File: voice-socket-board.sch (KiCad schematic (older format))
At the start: 296 parts, among them J1 JACK_MONO_SW, J2 JACK_MONO_SW, J3 JACK_MONO_SW, P1 CONN_01X03, P2 CONN_01X03, P3 CONN_02X05, P4 DDR3-DIMM, Q1 MMBT3904, Q10 MMBT3906, Q2 DMMT3904W, Q3 2N7002, Q4 2N7002, Q5 MMBT3904, Q6 MMBT3906, Q7 MMBT3904, Q8 MMBT3904, Q9 MMBT3904, SW1 SPST, SW10 SP3T, SW11 SP3T, SW12 SP3T, SW13 SP3T, SW14 SPST, SW15 TACT_SWITCH, SW16 SP3T, SW2 SPST, SW3 SP3T, SW4 SP3T, SW5 SPST, SW6 SPST, SW7 Switch_SPDT_x2, SW8 2P3T, SW9 SP3T, U1 LM833, U10 TL072-, U11 NE5534, U2 TL072-, U3 TL072-, U4 TL072-, U5 TL072-, U6 TL072-, U7 MAX9945, U8 CD4013, U9 TL072-

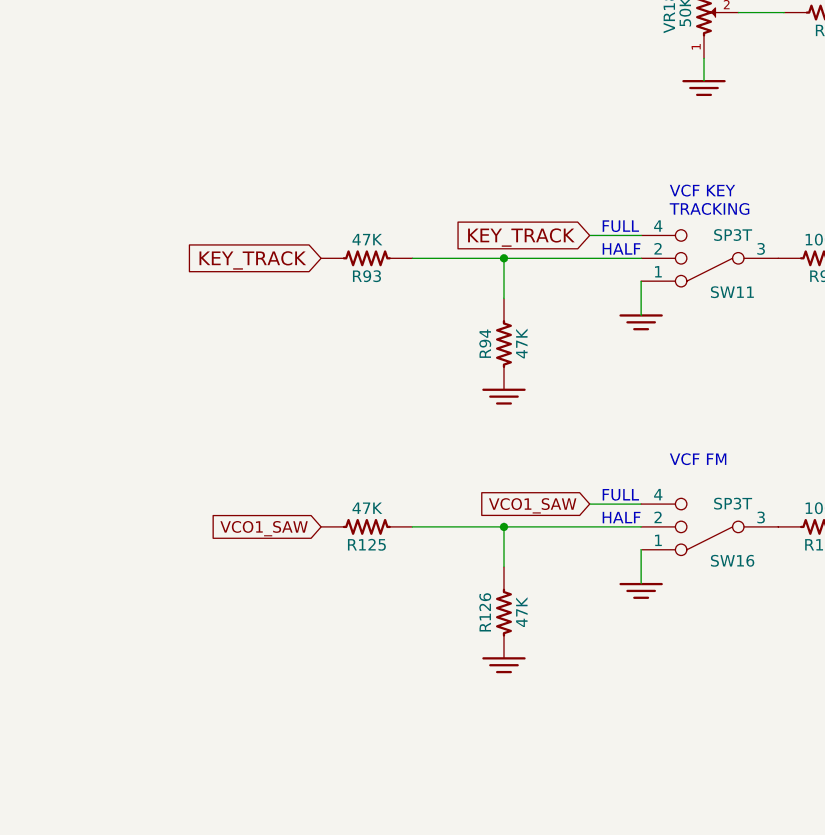
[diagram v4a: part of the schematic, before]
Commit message: changed FM and key tracking inputs into filter cutoff summer
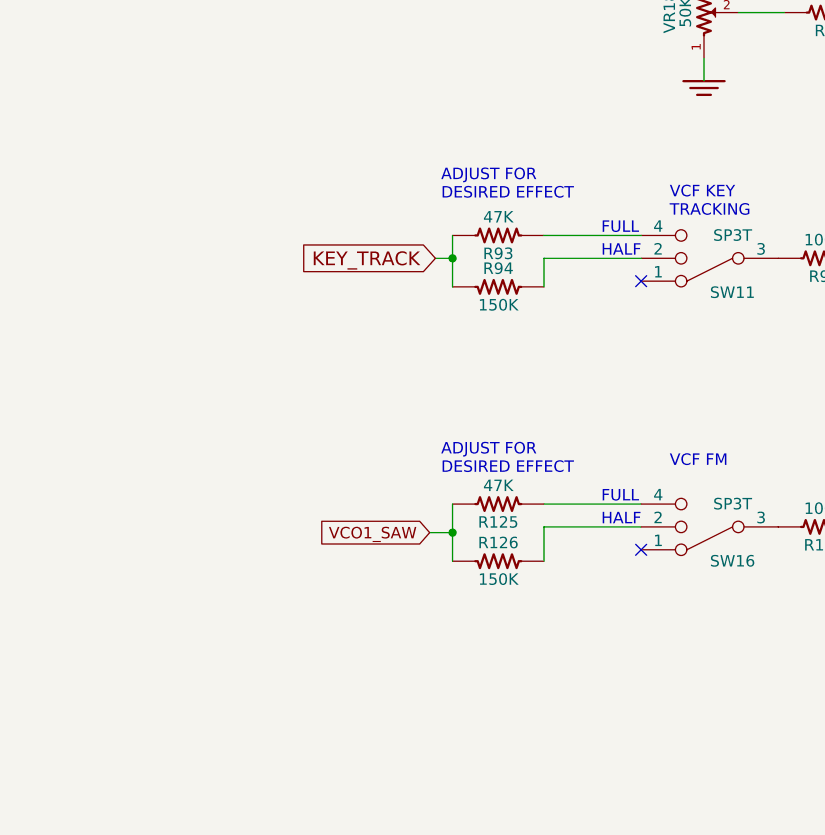
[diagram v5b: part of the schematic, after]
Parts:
- R126, R94: value 47K -> 150K
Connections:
- net GND: no longer R126.1, R94.1, SW11.1, SW16.1
- net KEY_TRACK: now also R94.1; no longer SW11.4
- net VCO1_SAW: now also R126.1; no longer SW16.4
- net at R94.2, SW11.2: no longer R93.1
- net at R126.2, SW16.2: no longer R125.1
- new net: R93.1, SW11.4
- new net: R125.1, SW16.4
- no-connect marks 11 -> 13
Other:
- note added: "ADJUST FOR \nDESIRED EFFECT\n"
- moved on the sheet: R125, R126, R93, R94
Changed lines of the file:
@@
 Text Notes 33525 16700 0    50   ~ 0
 OR SOME OTHER LOW OFFSET PRECISION OP AMP
-Text GLabel 18075 23925 0    60   Input ~ 0
-KEY_TRACK
 $Comp
 L SP3T SW11
@@
 $EndComp
 $Comp
-L GND_E #PWR0222
-U 1 1 566E42FA
-P 18300 24275
-F 0 "#PWR0222" V 18300 24275 30  0001 C CNN
-F 1 "GND_E" H 18300 24205 30  0001 C CNN
-F 2 "" H 18300 24275 60  0000 C CNN
-F 3 "" H 18300 24275 60  0000 C CNN
-	1    18300 24275
-	1    0    0    -1
-$EndComp
-$Comp
 L R_US R98
 U 1 1 566E8731
@@
 	0    1    1    0
 $EndComp
-Text GLabel 16900 24025 0    60   Input ~ 0
+Text GLabel 17400 24025 0    60   Input ~ 0
 KEY_TRACK
 $Comp
 L R_US R93
 U 1 1 566EB837
-P 17100 24025
-F 0 "R93" V 17180 24025 50  0000 C CNN
-F 1 "47K" V 17020 24025 50  0000 C CNN
-F 2 "MyModules:SM0603-R-JRL" H 17100 24025 60  0001 C CNN
-F 3 "" H 17100 24025 60  0000 C CNN
-	1    17100 24025
+P 17675 23925
+F 0 "R93" V 17755 23925 50  0000 C CNN
+F 1 "47K" V 17595 23925 50  0000 C CNN
+F 2 "MyModules:SM0603-R-JRL" H 17675 23925 60  0001 C CNN
+F 3 "" H 17675 23925 60  0000 C CNN
+	1    17675 23925
 	0    1    1    0
 $EndComp
@@
 L R_US R94
 U 1 1 566EBBBE
-P 17700 24400
-F 0 "R94" V 17780 24400 50  0000 C CNN
-F 1 "47K" V 17620 24400 50  0000 C CNN
-F 2 "MyModules:SM0603-R-JRL" H 17700 24400 60  0001 C CNN
-F 3 "" H 17700 24400 60  0000 C CNN
-	1    17700 24400
-	-1   0    0    1
-$EndComp
-$Comp
-L GND_E #PWR0223
-U 1 1 566ED5F9
-P 17700 24600
-F 0 "#PWR0223" V 17700 24600 30  0001 C CNN
-F 1 "GND_E" H 17700 24530 30  0001 C CNN
-F 2 "" H 17700 24600 60  0000 C CNN
-F 3 "" H 17700 24600 60  0000 C CNN
-	1    17700 24600
-	1    0    0    -1
+P 17675 24150
+F 0 "R94" V 17755 24150 50  0000 C CNN
+F 1 "150K" V 17595 24150 50  0000 C CNN
+F 2 "MyModules:SM0603-R-JRL" H 17675 24150 60  0001 C CNN
+F 3 "" H 17675 24150 60  0000 C CNN
+	1    17675 24150
+	0    -1   -1   0
 $EndComp
 Text Notes 18425 23850 0    50   ~ 0
@@
 Connection ~ 29875 16750
 Wire Wire Line
-	18300 24125 18300 24275
-Wire Wire Line
-	18300 23925 18075 23925
+	17875 23925 18300 23925
 Wire Wire Line
 	19300 24025 19575 24025
 Connection ~ 19575 24025
-Wire Wire Line
-	17300 24025 18300 24025
-Wire Wire Line
-	17700 24200 17700 24025
-Connection ~ 17700 24025
 Wire Wire Line
 	28125 10325 29025 10325
@@
 $EndComp
 $Comp
-L GND_E #PWR0242
-U 1 1 567C7030
-P 18300 25450
-F 0 "#PWR0242" V 18300 25450 30  0001 C CNN
-F 1 "GND_E" H 18300 25380 30  0001 C CNN
-F 2 "" H 18300 25450 60  0000 C CNN
-F 3 "" H 18300 25450 60  0000 C CNN
-	1    18300 25450
-	1    0    0    -1
-$EndComp
-$Comp
 L R_US R127
 U 1 1 567C7036
@@
 L R_US R125
 U 1 1 567C703D
-P 17100 25200
-F 0 "R125" V 17180 25200 50  0000 C CNN
-F 1 "47K" V 17020 25200 50  0000 C CNN
-F 2 "MyModules:SM0603-R-JRL" H 17100 25200 60  0001 C CNN
-F 3 "" H 17100 25200 60  0000 C CNN
-	1    17100 25200
+P 17675 25100
+F 0 "R125" V 17755 25100 50  0000 C CNN
+F 1 "47K" V 17595 25100 50  0000 C CNN
+F 2 "MyModules:SM0603-R-JRL" H 17675 25100 60  0001 C CNN
+F 3 "" H 17675 25100 60  0000 C CNN
+	1    17675 25100
 	0    1    1    0
 $EndComp
@@
 L R_US R126
 U 1 1 567C7043
-P 17700 25575
-F 0 "R126" V 17780 25575 50  0000 C CNN
-F 1 "47K" V 17620 25575 50  0000 C CNN
-F 2 "MyModules:SM0603-R-JRL" H 17700 25575 60  0001 C CNN
-F 3 "" H 17700 25575 60  0000 C CNN
-	1    17700 25575
-	-1   0    0    1
-$EndComp
-$Comp
-L GND_E #PWR0243
-U 1 1 567C7049
-P 17700 25775
-F 0 "#PWR0243" V 17700 25775 30  0001 C CNN
-F 1 "GND_E" H 17700 25705 30  0001 C CNN
-F 2 "" H 17700 25775 60  0000 C CNN
-F 3 "" H 17700 25775 60  0000 C CNN
-	1    17700 25775
-	1    0    0    -1
+P 17675 25350
+F 0 "R126" V 17755 25350 50  0000 C CNN
+F 1 "150K" V 17595 25350 50  0000 C CNN
+F 2 "MyModules:SM0603-R-JRL" H 17675 25350 60  0001 C CNN
+F 3 "" H 17675 25350 60  0000 C CNN
+	1    17675 25350
+	0    -1   -1   0
 $EndComp
 Text Notes 18425 25025 0    50   ~ 0
 VCF FM\n\n
 Wire Wire Line
-	18300 25300 18300 25450
-Wire Wire Line
-	18300 25100 18075 25100
-Wire Wire Line
-	17300 25200 18300 25200
-Wire Wire Line
-	17700 25375 17700 25200
-Connection ~ 17700 25200
+	17875 25100 18300 25100
 Text Notes 18125 25100 0    50   ~ 0
 FULL\n
 Text Notes 18125 25200 0    50   ~ 0
 HALF
-Text GLabel 16900 25200 0    50   Input ~ 0
-VCO1_SAW
-Text GLabel 18075 25100 0    50   Input ~ 0
+Text GLabel 17375 25225 0    50   Input ~ 0
 VCO1_SAW
 Wire Wire Line
@@
 $EndComp
 $Comp
-L GND_E #PWR0246
+L GND_E #PWR0244
 U 1 1 567F81C4
 P 26575 23750
-F 0 "#PWR0246" V 26575 23750 30  0001 C CNN
+F 0 "#PWR0244" V 26575 23750 30  0001 C CNN
 F 1 "GND_E" H 26575 23680 30  0001 C CNN
 F 2 "" H 26575 23750 60  0000 C CNN
@@
 Wire Wire Line
 	27325 25300 27325 25575
+Wire Wire Line
+	18300 24025 17875 24025
+Wire Wire Line
+	17875 24025 17875 24150
+Wire Wire Line
+	17475 23925 17475 24150
+Wire Wire Line
+	17400 24025 17475 24025
+Connection ~ 17475 24025
+NoConn ~ 18300 24125
+Text Notes 17425 23775 0    50   ~ 0
+ADJUST FOR \nDESIRED EFFECT\n
+NoConn ~ 18300 25300
+Wire Wire Line
+	18300 25200 17875 25200
+Wire Wire Line
+	17875 25200 17875 25350
+Wire Wire Line
+	17475 25100 17475 25350
+Wire Wire Line
+	17375 25225 17475 25225
+Connection ~ 17475 25225
+Text Notes 17425 24975 0    50   ~ 0
+ADJUST FOR \nDESIRED EFFECT\n
 $EndSCHEMATC

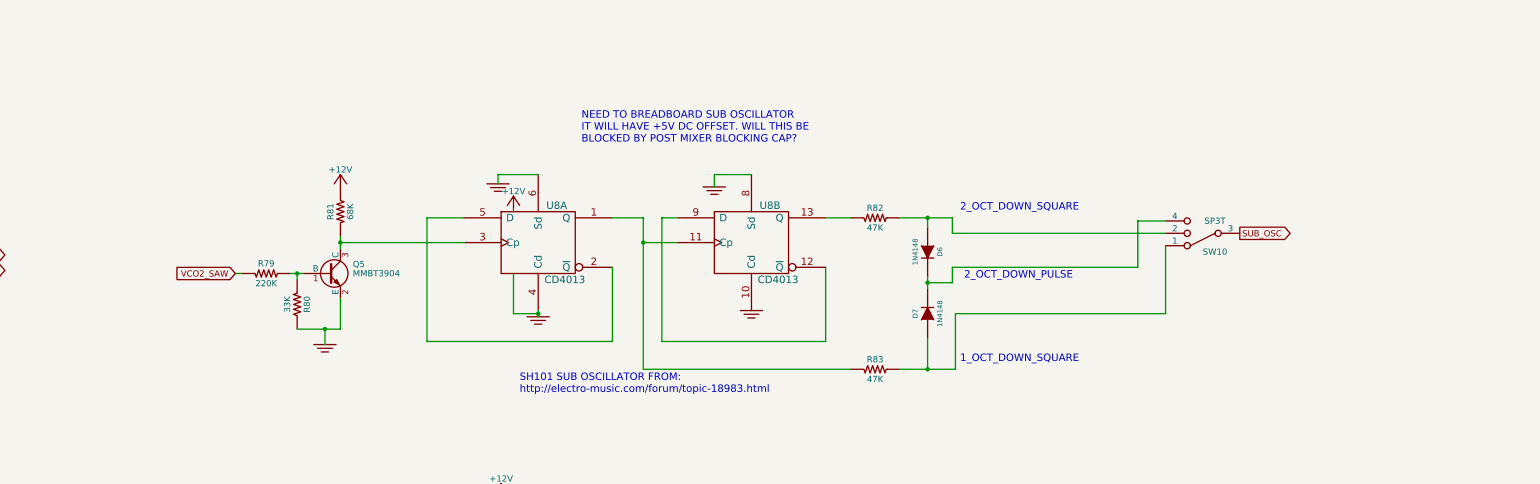
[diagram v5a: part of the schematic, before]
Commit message: changed CD4013 suboscillator clock input and added levelshiefter on sub osc output
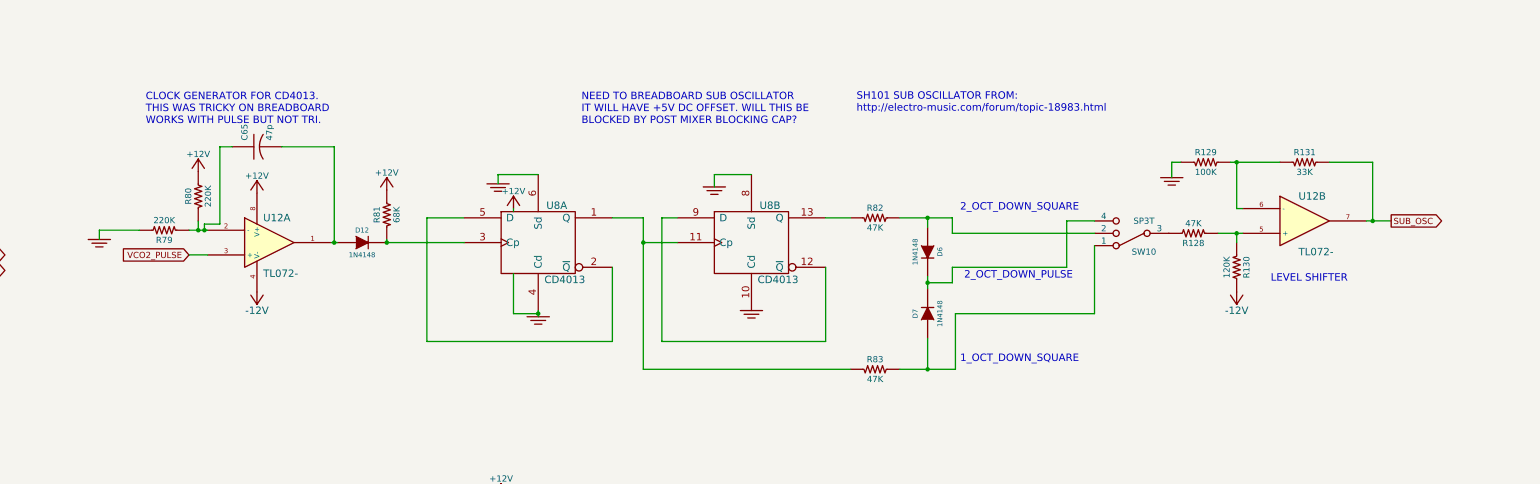
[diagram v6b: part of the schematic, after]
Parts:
- removed Q5: MMBT3904, MyModules:SOT23-132-JRL, symbol MMBT3904
- added C65: 47p, MyModules:SM0603-C-JRL, symbol C_US
- added D12: 1N4148, MyModules:SOD323-JRL, symbol DIODE
- added R128: 47K, MyModules:SM0603-R-JRL, symbol R_US
- added R129: 100K, MyModules:SM0603-R-JRL, symbol R_US
- added R130: 120K, MyModules:SM0603-R-JRL, symbol R_US
- added R131: 33K, MyModules:SM0603-R-JRL, symbol R_US
- added U12: TL072-, MyModules:TSSOP8-JRL, symbol TL072-
- R80: value 33K -> 220K
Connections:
- net +12V: now also R80.2, U12.8 (V+)
- net -12V: now also R130.2, U12.4 (V-)
- net GND: now also R79.2, R129.1; no longer R80.2
- net SUB_OSC: now also R131.2, U12.7; no longer SW10.3
- net VCO2_PULSE: now also U12.3 (+)
- net VCO2_SAW: no longer R79.1
- net at R80.1: now also R79.1, C65.1, U12.2 (-); no longer R79.2
- net at R81.1, U8.3 (Cp): now also D12.2 (K)
- new net: R128.2, SW10.3
- new net: R128.1, R130.1, U12.5 (+)
- new net: R129.2, R131.1, U12.6 (-)
- new net: C65.2, D12.1 (A), U12.1
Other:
- note added: "CLOCK GENERATOR FOR CD4013. \nTHIS WAS TRICKY ON BREADBOARD\nWORKS WITH PULSE BUT NOT TRI."
- note added: "LEVEL SHIFTER"
- moved on the sheet: R79, R80, R81, SW10

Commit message: more silkscreen labelling, almost ready to plot gerbers
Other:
- note added: "NEED TO BREADBOARD SUB OSCILLATOR\nIT WILL HAVE +5V DC OFFSET. WILL THIS BE \nBLOCKED BY POST MIXER BLOCKING CAP?\nSEEMS OK - LOOKED AT OUTPUT OF MC-202\nSUB-OSCILLATOR AND IT IS IDENTICAL TO\nBREADBOARDED SUB-OSCILLATOR"
- note removed: "NEED TO BREADBOARD SUB OSCILLATOR\nIT WILL HAVE +5V DC OFFSET. WILL THIS BE \nBLOCKED BY POST MIXER BLOCKING CAP?"
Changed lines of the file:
@@
 $EndComp
 Text Notes 19225 17350 0    60   ~ 0
-NEED TO BREADBOARD SUB OSCILLATOR\nIT WILL HAVE +5V DC OFFSET. WILL THIS BE \nBLOCKED BY POST MIXER BLOCKING CAP?
+NEED TO BREADBOARD SUB OSCILLATOR\nIT WILL HAVE +5V DC OFFSET. WILL THIS BE \nBLOCKED BY POST MIXER BLOCKING CAP?\nSEEMS OK - LOOKED AT OUTPUT OF MC-202\nSUB-OSCILLATOR AND IT IS IDENTICAL TO\nBREADBOARDED SUB-OSCILLATOR
 Text Notes 21450 17250 0    60   ~ 0
 SH101 SUB OSCILLATOR FROM:\nhttp://electro-music.com/forum/topic-18983.html
